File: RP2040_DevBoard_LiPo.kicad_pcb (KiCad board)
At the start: 2 copper layers, 24 x 50 mm, 55 parts, among them J1 HRO_TYPE-C-31-M-14, J2 Conn_01x18, J3 Conn_01x18, J4 Battery, Q1 DMP2045U, SW1 SW_Push, SW2 SW_Push, SW3 Vin_Switch, U1 USBLC6-2SC6, U2 W25Q128JVS, U3 SOT23-5 200mA 3.3V, U4 TP4056, U5 RP2040, Y1 Crystal_GND23

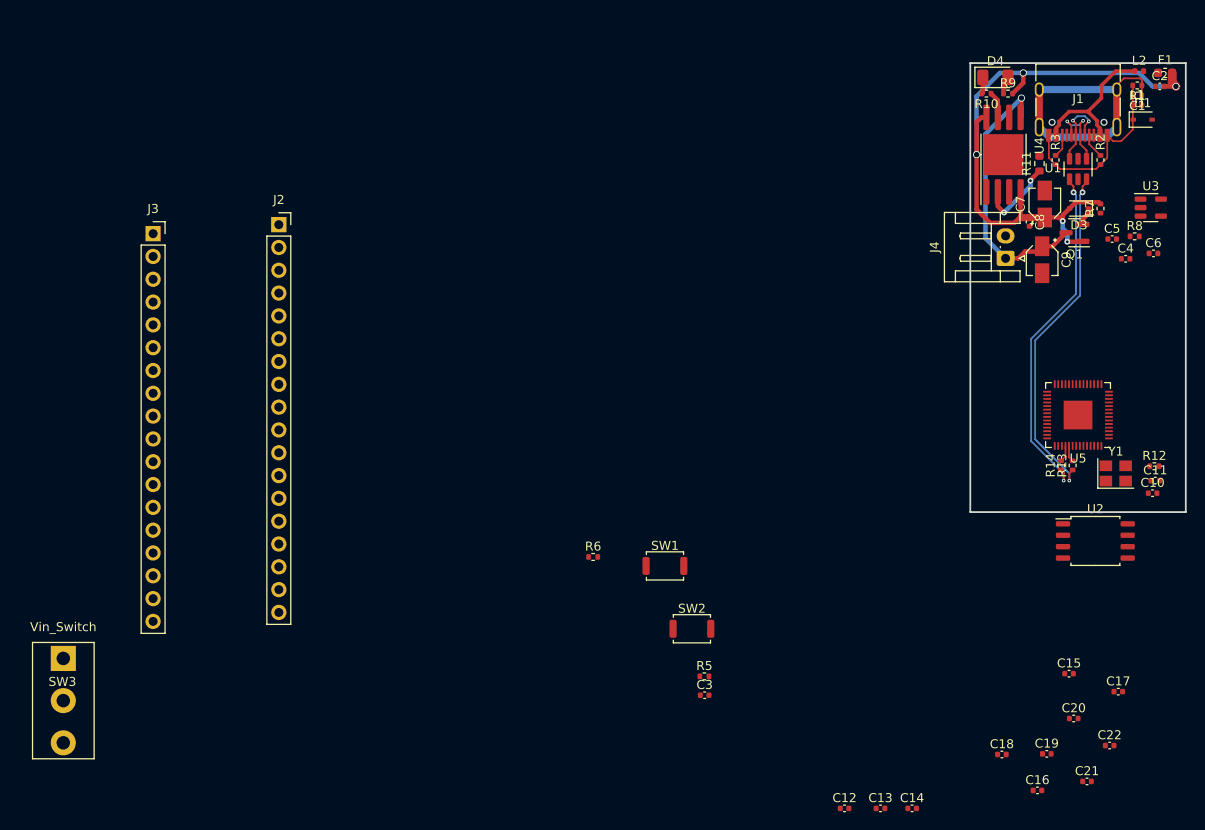
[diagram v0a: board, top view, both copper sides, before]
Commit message: Finished routing Featherboard
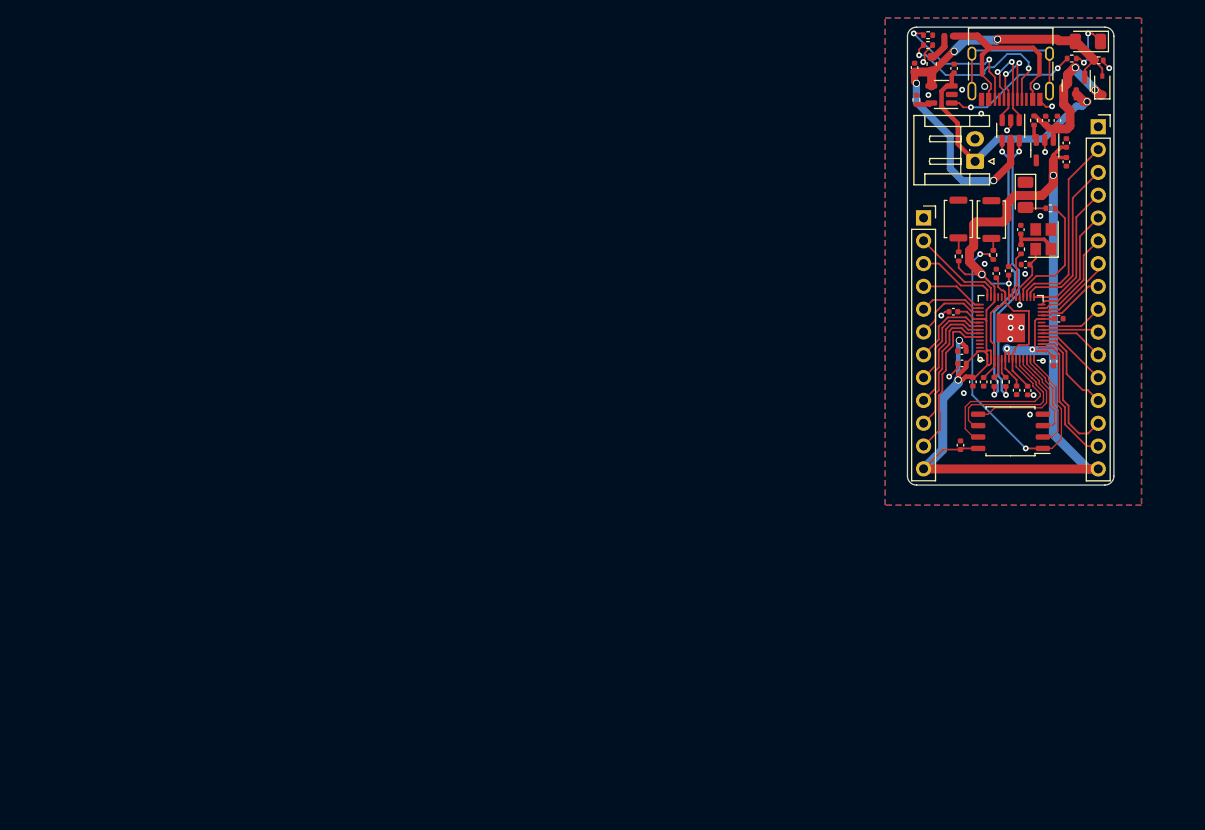
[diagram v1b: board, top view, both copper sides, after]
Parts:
- removed C21, C22: 100nF, Capacitor_SMD:C_0402_1005Metric
- removed D4: LED, LED_SMD:LED_1206_3216Metric
- removed J4: Battery, Connector_JST:JST_EH_S2B-EH_1x02_P2.50mm_Horizontal
- removed L2: BLM15PX121SN1D, Inductor_SMD:L_0402_1005Metric
- removed R13, R14: 27, Resistor_SMD:R_0402_1005Metric
- removed SW3: Vin_Switch, Buggy_Footprints:switch123
- added D2: D_Schottky, Diode_SMD:D_SOD-323, F.Cu at (181.7, 26.5)
- added J6: Conn_01x12, Connector_PinSocket_2.54mm:PinSocket_1x12_P2.54mm_Vertical, F.Cu at (161.8, 41.2)
- added R4: 10k, Resistor_SMD:R_0402_1005Metric, F.Cu at (181.3, 23.7)
- C1, C6: value 100nF -> 10uF
- C10: value 22pF -> 1u
- C11: value 22pF -> 100nF
- C12, C15, C5: value 1u -> 100nF
- C13: value 100nF -> 1u
- C3: value 100nF -> 1uF
- C7: value 10 uF -> 22pF; footprint Capacitor_SMD:CP_Elec_3x5.3 -> Capacitor_SMD:C_0402_1005Metric
- C8: value 4.7 uF -> 22pF
- C9: value 10 uF -> 100nF; footprint Capacitor_SMD:CP_Elec_3x5.3 -> Capacitor_SMD:C_0402_1005Metric
- D1: value BSD3C051V -> LED; footprint Diode_SMD:D_SOD-323 -> LED_SMD:LED_1206_3216Metric
- D3: value D_Schottky -> LED; footprint Diode_SMD:D_SOD-323 -> LED_SMD:LED_1206_3216Metric
- J2: value Conn_01x18 -> Conn_01x16; footprint Connector_PinSocket_2.54mm:PinSocket_1x18_P2.54mm_Vertical -> Connector_PinSocket_2.54mm:PinSocket_1x16_P2.54mm_Vertical
- J3: value Conn_01x18 -> Battery; footprint Connector_PinSocket_2.54mm:PinSocket_1x18_P2.54mm_Vertical -> Connector_JST:JST_EH_S2B-EH_1x02_P2.50mm_Horizontal
- Q1: value DMP2045U -> SI2301A
- R1: value 1 MOhm -> 5k1
- R10: value 1.5k -> 27
- R11: value 5k -> 1k; footprint Resistor_SMD:R_0603_1608Metric -> Resistor_SMD:R_0402_1005Metric
- R3: value 5k1 -> 470
- R5: value 1k -> 10k
- R6: value 1k -> 2k
- R7: value 1.5k -> 1k
- R8: value 10k -> 1k
- R9: value 470 -> 27
- U2: value W25Q128JVS -> SOT23-5 200mA 3.3V; footprint Package_SO:SOIC-8_5.23x5.23mm_P1.27mm -> Package_TO_SOT_SMD:SOT-23-5
- U3: value SOT23-5 200mA 3.3V -> TP4054
- U4: value TP4056 -> RP2040; footprint Package_SO:SOP-8-1EP_4.57x4.57mm_P1.27mm_EP4.57x4.45mm -> Package_DFN_QFN:QFN-56-1EP_7x7mm_P0.4mm_EP3.2x3.2mm
- U5: value RP2040 -> W25Q128JVS; footprint Package_DFN_QFN:QFN-56-1EP_7x7mm_P0.4mm_EP3.2x3.2mm -> Package_SO:SOIC-8_5.23x5.23mm_P1.27mm
- moved J2 91.9 mm to (181.2, 31.1)
- moved J3 91.9 mm to (167.5, 35.0), turned to 90 degrees
- moved C3 75.1 mm to (176.7, 30.4), turned to 90 degrees
- moved R5 72.0 mm to (174.1, 30.4), turned to 90 degrees
- moved R6 62.3 mm to (161.0, 28.1), turned to 90 degrees
- moved C13 61.5 mm to (171.3, 47.1), turned to 90 degrees
- moved SW2 54.4 mm to (165.7, 41.4), turned to -90 degrees
- moved SW1 53.0 mm to (169.3, 41.4), turned to -90 degrees
- moved C16 52.6 mm to (176.9, 52.5), turned to 180 degrees
- moved C14 52.2 mm to (176.3, 57.2), turned to 90 degrees
- moved C12 50.0 mm to (168.5, 59.5), turned to 90 degrees
- moved U2 43.9 mm to (175.3, 33.7), turned to -90 degrees
- moved C20 42.8 mm to (166.1, 56.1)
- moved C15 42.3 mm to (165.1, 51.7)
- moved C18 41.6 mm to (167.3, 59.5), turned to 90 degrees
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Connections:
- C1 pad 1: Earth -> GND
- C1 pad 2: GNDPWR -> +5V
- C10 pad 1: XIN -> +1V1
- C11 pad 1: Net-(C11-Pad1) -> GND
- C11 pad 2: GND -> +1V1
- C12 pad 1: +1V1 -> GND
- C12 pad 2: GND -> +1V1
- C13 pad 1: GND -> +3V3
- C13 pad 2: +1V1 -> GND
- C14 pad 2: +1V1 -> +3V3
- C15 pad 1: RUN -> GND
- C15 pad 2: GND -> +3V3
- C16 pad 2: RUN -> +3V3
- C17 pad 2: RUN -> +3V3
- C18 pad 2: RUN -> +3V3
- C19 pad 2: RUN -> +3V3
- C2 pad 1: GND -> /VSRC
- C2 pad 2: +5V -> GND
- C20 pad 2: RUN -> +3V3
- C3 pad 1: GND -> /VSRC
- C3 pad 2: RUN -> GND
- C4 pad 1: /VSRC -> +3V3
- C5 pad 1: RUN -> GND
- C5 pad 2: GND -> +3V3
- C6 pad 1: GND -> +BATT
- C6 pad 2: RUN -> GND
- C7 pad 1: +5V -> XIN
- C8 pad 1: +5V -> Net-(C8-Pad1)
- C9 pad 1: Charge -> GND
- C9 pad 2: GND -> +3V3
- D1 pad 1: GNDPWR -> GND
- D1 pad 2: GND -> Net-(D1-Pad2)
- D3 pad 1: /VSRC -> Net-(D3-Pad1)
- J1 pad A1: GNDPWR -> GND
- J1 pad A12: GNDPWR -> GND
- J1 pad B1: GNDPWR -> GND
- J1 pad B12: GNDPWR -> GND
- J1 pad S1: Earth -> unconnected-(J1-PadS1)
- J2 pad 1: RUN -> GND
- J2 pad 10: /GPIO8 -> /GPIO5
- J2 pad 11: /GPIO9 -> /GPIO4
- J2 pad 12: /GPIO10 -> /GPIO3
- J2 pad 13: /GPIO11 -> /GPIO2
- J2 pad 14: /GPIO12 -> /GPIO1
- J2 pad 15: /GPIO13 -> /GPIO0
- J2 pad 16: /GPIO14 -> +3V3
- J2 pad 2: /GPIO0 -> /GPIO14
- J2 pad 3: /GPIO1 -> /GPIO13
- J2 pad 4: /GPIO2 -> /GPIO12
- J2 pad 5: /GPIO3 -> /GPIO11
- J2 pad 6: /GPIO4 -> /GPIO10
- J2 pad 7: /GPIO5 -> /GPIO9
- J2 pad 8: /GPIO6 -> /GPIO8
- J2 pad 9: /GPIO7 -> /GPIO6
- J3 pad 1: RUN -> +BATT
- J3 pad 2: /GPIO29 -> GND
- L1 pad 1: GNDPWR -> VBUS
- L1 pad 2: GND -> Net-(F1-Pad1)
- Q1 pad 3: Charge -> +BATT
- R1 pad 1: Earth -> /CC1
- R1 pad 2: GNDPWR -> GND
- R10 pad 1: Net-(R10-Pad1) -> USB_D-
- R10 pad 2: Net-(D4-Pad1) -> /DN
- R11 pad 1: Net-(R11-Pad1) -> /BOOT
- R11 pad 2: GND -> QSPI_SS
- R12 pad 1: Net-(C11-Pad1) -> /RESET
- R12 pad 2: XOUT -> +3V3
- R2 pad 1: /CC1 -> /CC2
- R2 pad 2: GNDPWR -> GND
- R3 pad 1: /CC2 -> Net-(D1-Pad2)
- R3 pad 2: GNDPWR -> /GPIO15
- R5 pad 1: /BOOT -> /ENABLE
- R5 pad 2: QSPI_SS -> /VSRC
- R6 pad 1: /RESET -> Net-(R6-Pad1)
- R6 pad 2: RUN -> GND
- R7 pad 1: GND -> Net-(R7-Pad1)
- R7 pad 2: +5V -> Net-(D3-Pad1)
- R8 pad 1: /VSRC -> Net-(C8-Pad1)
- R8 pad 2: /ENABLE -> XOUT
- R9 pad 1: Net-(D4-Pad2) -> USB_D+
- R9 pad 2: +5V -> /DP
- U2 pad 1: QSPI_SS -> /VSRC
- U2 pad 2: QSPI_SD1 -> GND
- U2 pad 3: QSPI_SD2 -> /ENABLE
- U2 pad 4: GND -> unconnected-(U2-Pad4)
- U2 pad 5: QSPI_SD0 -> +3V3
- U3 pad 1: /VSRC -> Net-(R7-Pad1)
- U3 pad 3: /ENABLE -> +BATT
- U3 pad 4: unconnected-(U3-Pad4) -> +5V
- U3 pad 5: RUN -> Net-(R6-Pad1)
- U4 pad 1: GND -> +3V3
- U4 pad 2: Net-(R11-Pad1) -> /GPIO0
- U4 pad 3: GND -> /GPIO1
- U4 pad 4: +5V -> /GPIO2
- U4 pad 5: Charge -> /GPIO3
- U4 pad 6: unconnected-(U4-Pad6) -> /GPIO4
- U4 pad 7: Net-(R10-Pad1) -> /GPIO5
- U4 pad 8: +5V -> /GPIO6
- U4 pad 9: (no net) -> /GPIO7
- U5 pad 1: RUN -> QSPI_SS
- U5 pad 2: /GPIO0 -> QSPI_SD1
- U5 pad 3: /GPIO1 -> QSPI_SD2
- U5 pad 4: /GPIO2 -> GND
- U5 pad 5: /GPIO3 -> QSPI_SD0
- U5 pad 6: /GPIO4 -> QSPI_SCLK
- U5 pad 7: /GPIO5 -> QSPI_SD3
- U5 pad 8: /GPIO6 -> +3V3
- Y1 pad 1: Net-(C11-Pad1) -> Net-(C8-Pad1)
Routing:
- net +3V3: track 0.00 -> 159.9 mm, vias 0 -> 7
- net QSPI_SS: track 0.00 -> 40.8 mm, vias 0 -> 2
- net Earth: track 31.9 -> 0.00 mm
- net Charge: track 30.5 -> 0.00 mm, vias 1 -> 0
- net +BATT: track 0.00 -> 29.1 mm, vias 0 -> 1
- net +1V1: track 0.00 -> 26.7 mm
- net /GPIO14: track 0.00 -> 21.4 mm
- net GNDPWR: track 21.2 -> 0.00 mm
- net +5V: track 70.7 -> 51.6 mm, vias 5 -> 4
- net /GPIO13: track 0.00 -> 18.7 mm
- net QSPI_SD3: track 0.00 -> 18.4 mm
- net /CC1: track 2.76 -> 20.4 mm, vias 0 -> 2
- net /GPIO26: track 0.00 -> 17.4 mm
- net unconnected-(J1-PadS1): track 0.00 -> 17.3 mm
- net QSPI_SCLK: track 0.00 -> 17.2 mm
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- added copper zone on B.Cu, net GND
- added copper zone on F.Cu, net GND
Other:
- board size 24 x 50 mm -> 23 x 51 mm

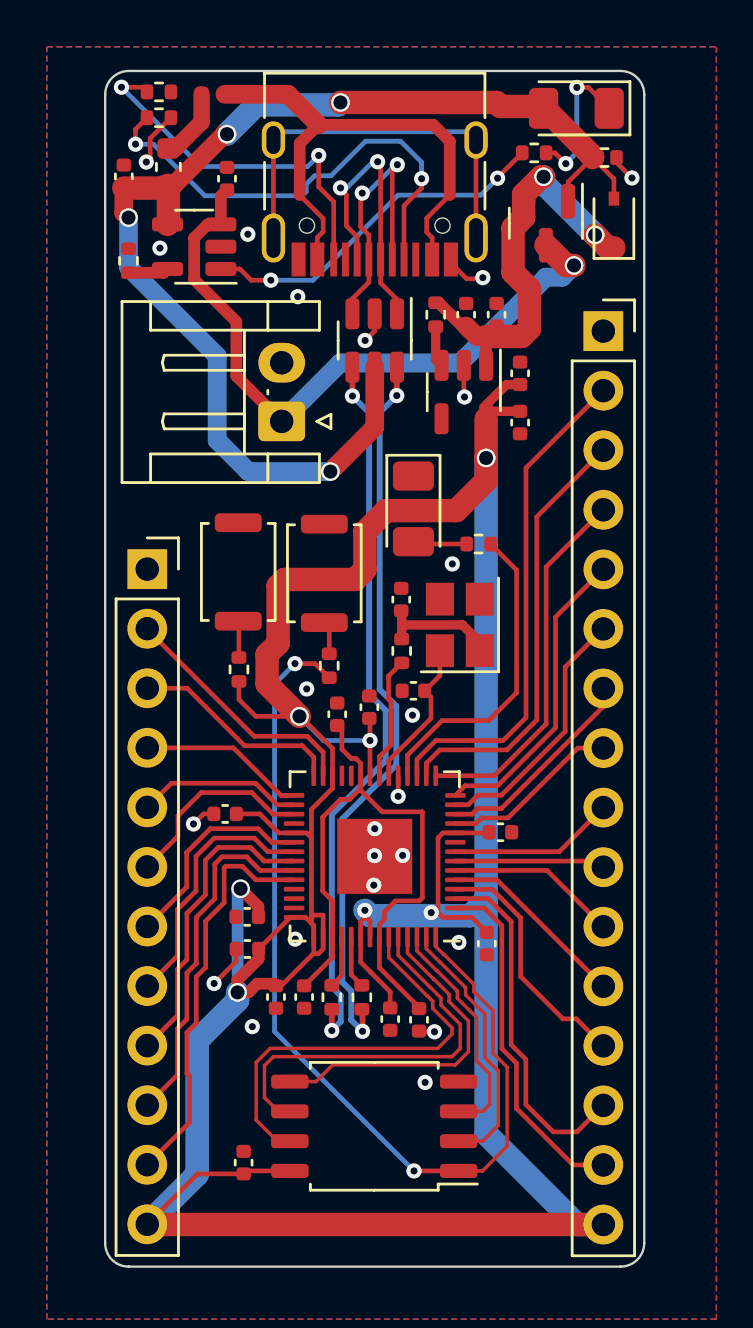
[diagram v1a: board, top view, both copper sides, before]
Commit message: added adjustments to vias around the board
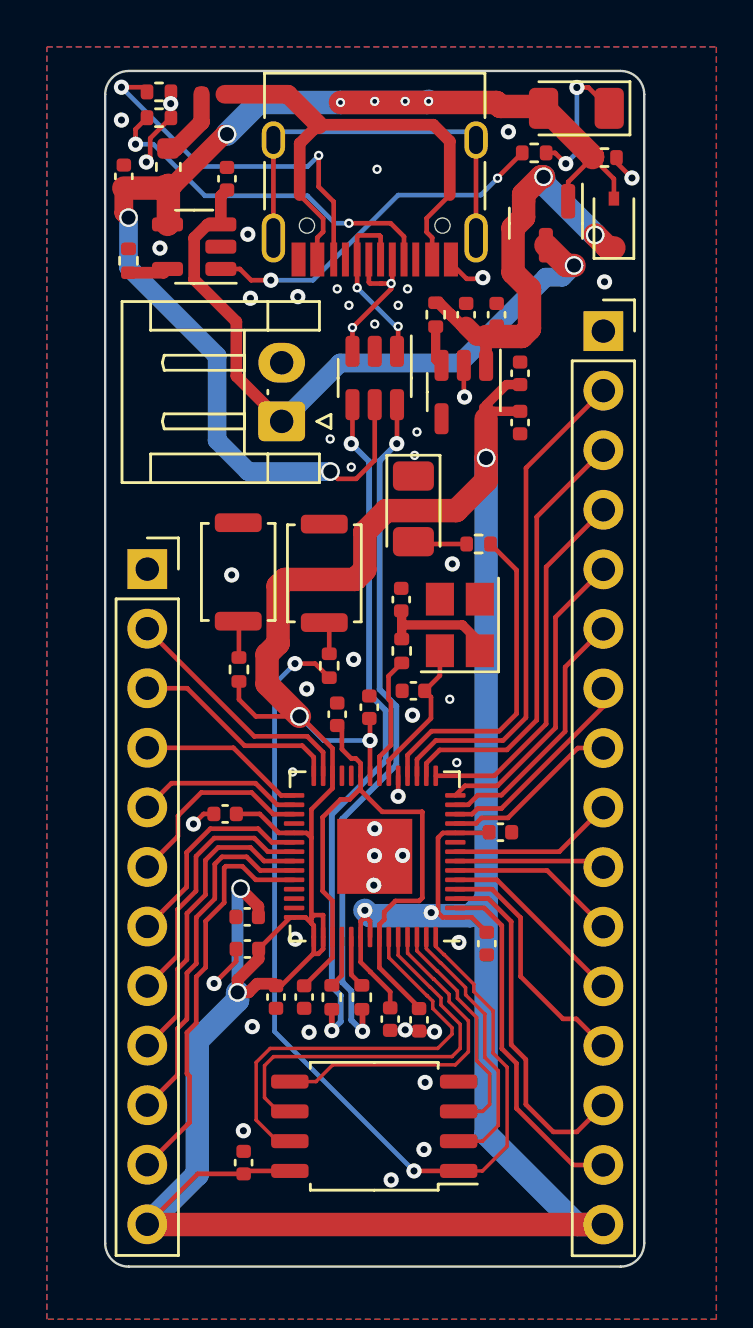
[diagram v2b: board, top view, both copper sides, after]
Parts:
- moved U1 1.60 mm to (171.5, 33.1)
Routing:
- net D-: track 11.7 -> 6.57 mm
- net /CC1: track 20.4 -> 15.4 mm
- net D+: track 12.2 -> 7.71 mm
- net +5V: track 51.6 -> 54.9 mm, vias 4 -> 7
- net USB_D+: track 31.2 -> 29.6 mm
- net USB_D-: track 31.1 -> 29.5 mm
- net GND: track 12.4 -> 11.1 mm, vias 23 -> 47
- net /GPIO15: track 13.4 -> 14.0 mm
